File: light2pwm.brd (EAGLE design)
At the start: 55.5 x 47 mm, 8 parts, among them IC2 QUAD_OPAMPP

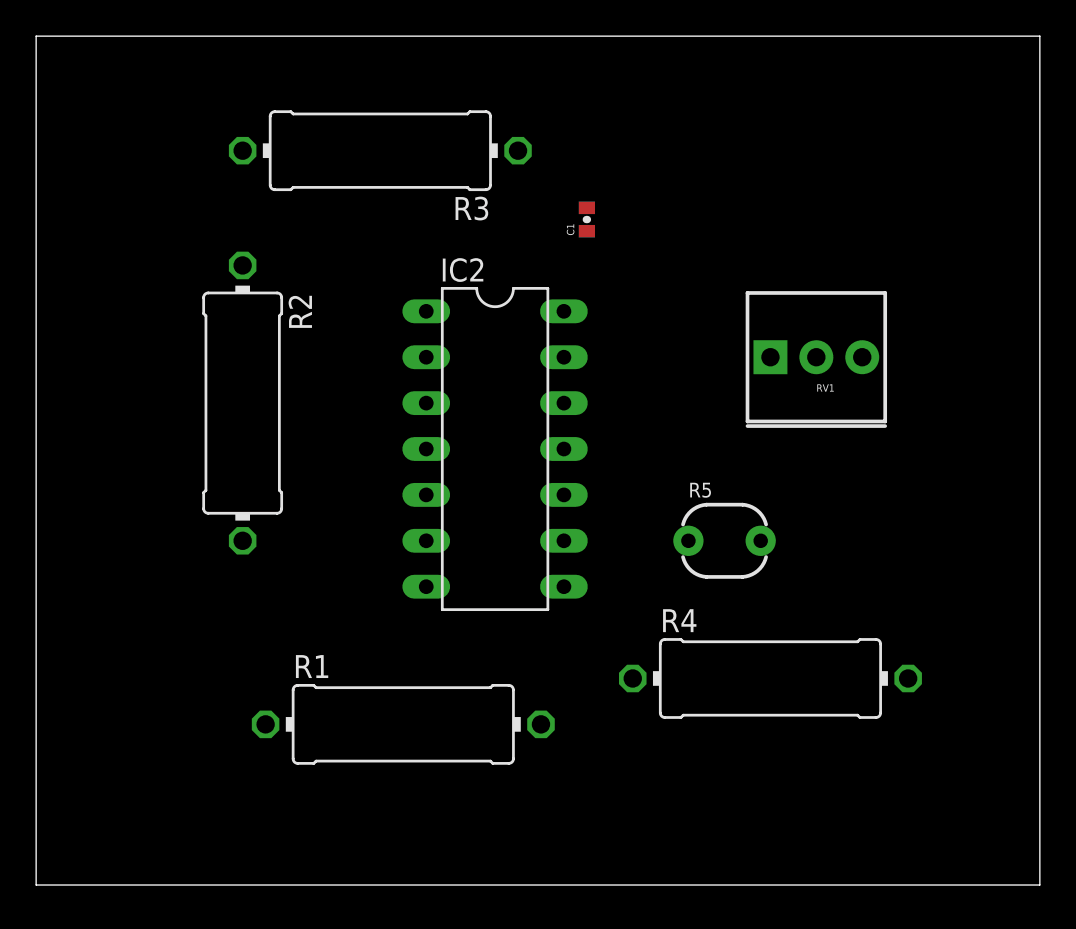
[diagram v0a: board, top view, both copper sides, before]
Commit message: pwm output pin added, next add transistor
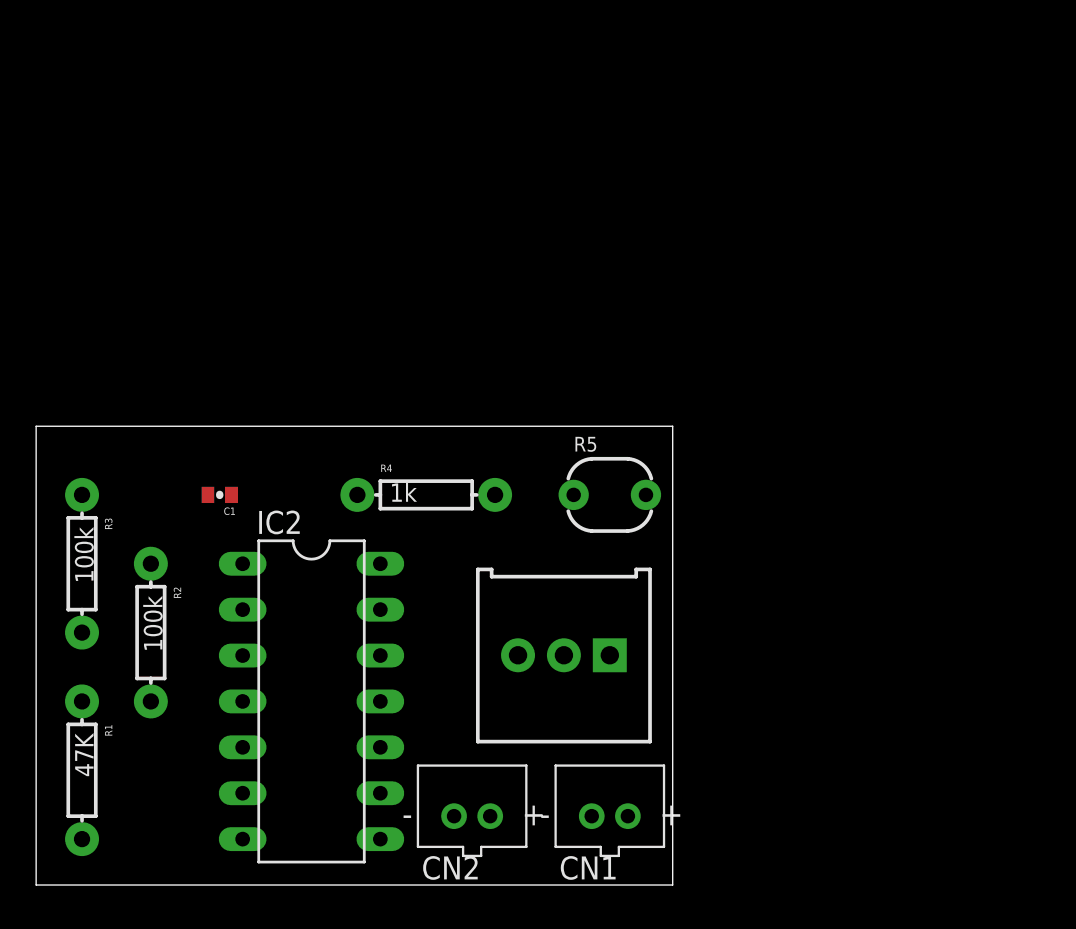
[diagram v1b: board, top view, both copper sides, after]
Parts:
- removed RV1: 10k, SparkFun-Electromechanical:3362U
- added CN1, CN2: (no value), adafruit:JST-PH-2-THM
- added R6: 10K, SparkFun-Electromechanical:3386U
- R1, R2, R3, R4: device adafruit:0414/15 -> SparkFun-Resistors:AXIAL-0.3EZ
- moved R3 28.2 mm to (2.54, 17.8), turned to 270 degrees
- moved C1 25.4 mm to (10.2, 21.6), turned to 180 degrees
- moved R4 21.6 mm to (21.6, 21.6)
- moved R1 18.0 mm to (2.54, 6.35), turned to 270 degrees
- moved IC2 17.3 mm to (15.2, 10.2)
- moved R2 13.7 mm to (6.35, 14.0)
- moved R5 6.84 mm to (31.8, 21.6)
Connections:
- new net N$7: CN2.2, IC2.8
- net GND: now also CN1.1, CN2.1, R4.P$2, R6.3; no longer R4.2, RV1.P$3
- net N$1: now also R1.P$1, R2.P$2; no longer R1.1, R2.2
- net N$2: now also R1.P$2; no longer R1.2
- net N$3: now also R2.P$1, R3.P$2; no longer R2.1, R3.2
- net N$4: now also R6.2; no longer RV1.P$2
- net N$5: now also R3.P$1; no longer R3.1
- net N$8: now also R4.P$1; no longer R4.1
- net VCC: now also CN1.2, R6.1; no longer RV1.P$1
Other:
- board size 55.5 x 47 mm -> 35.2 x 25.4 mm
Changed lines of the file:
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@@
 <board>
 <plain>
-<wire x1="0" y1="0" x2="55.55" y2="0" width="0" layer="20"/>
-<wire x1="55.55" y1="0" x2="55.55" y2="46.98" width="0" layer="20"/>
-<wire x1="55.55" y1="46.98" x2="0" y2="46.98" width="0" layer="20"/>
-<wire x1="0" y1="46.98" x2="0" y2="0" width="0" layer="20"/>
+<wire x1="0" y1="0" x2="35.23" y2="0" width="0" layer="20"/>
+<wire x1="35.23" y1="0" x2="35.23" y2="25.39" width="0" layer="20"/>
+<wire x1="35.23" y1="25.39" x2="0" y2="25.39" width="0" layer="20"/>
+<wire x1="0" y1="25.39" x2="0" y2="0" width="0" layer="20"/>
 </plain>
 <attributes>
@@
 </autorouter>
 <elements>
-<element name="C1" library="SparkFun-Retired" package="0402-CAP" value="10nF" x="30.48" y="36.83" rot="R90">
-<attribute name="PROD_ID" value="CAP-00867" x="30.48" y="36.83" size="1.778" layer="27" rot="R90" display="off"/>
+<element name="C1" library="SparkFun-Retired" package="0402-CAP" value="10nF" x="10.16" y="21.59" rot="R180">
+<attribute name="PROD_ID" value="CAP-00867" x="10.16" y="21.59" size="1.778" layer="27" rot="R180" display="off"/>
 </element>
-<element name="IC2" library="adafruit" package="DIL14" value="QUAD_OPAMPP" x="25.4" y="24.13" rot="R270"/>
-<element name="R1" library="adafruit" package="0414/15" value="47K" x="20.32" y="8.89"/>
-<element name="R2" library="adafruit" package="0414/15" value="100k" x="11.43" y="26.67" rot="R270"/>
-<element name="R3" library="adafruit" package="0414/15" value="100k" x="19.05" y="40.64" rot="R180"/>
-<element name="R4" library="adafruit" package="0414/15" value="1k" x="40.64" y="11.43"/>
-<element name="R5" library="SparkFun-Sensors" package="PHOTOCELL" value="PHOTOCELLPTH" x="38.1" y="19.05"/>
-<element name="RV1" library="SparkFun-Electromechanical" package="3362U" value="10k" x="40.64" y="26.67"/>
+<element name="IC2" library="adafruit" package="DIL14" value="QUAD_OPAMPP" x="15.24" y="10.16" rot="R270"/>
+<element name="R1" library="SparkFun-Resistors" package="AXIAL-0.3EZ" value="47K" x="2.54" y="6.35" rot="R270"/>
+<element name="R2" library="SparkFun-Resistors" package="AXIAL-0.3EZ" value="100k" x="6.35" y="13.97" rot="R270"/>
+<element name="R3" library="SparkFun-Resistors" package="AXIAL-0.3EZ" value="100k" x="2.54" y="17.78" rot="R270"/>
+<element name="R4" library="SparkFun-Resistors" package="AXIAL-0.3EZ" value="1k" x="21.59" y="21.59"/>
+<element name="R5" library="SparkFun-Sensors" package="PHOTOCELL" value="PHOTOCELLPTH" x="31.75" y="21.59"/>
+<element name="R6" library="SparkFun-Electromechanical" package="3386U" value="10K" x="29.21" y="12.7" rot="R180"/>
+<element name="CN1" library="adafruit" package="JST-PH-2-THM" value="" x="31.75" y="3.81"/>
+<element name="CN2" library="adafruit" package="JST-PH-2-THM" value="" x="24.13" y="3.81"/>
 </elements>
 <signals>
@@
 <signal name="N$1">
 <contactref element="IC2" pad="3"/>
-<contactref element="R1" pad="1"/>
-<contactref element="R2" pad="2"/>
-<wire x1="11.43" y1="19.05" x2="21.59" y2="26.67" width="0" layer="19" extent="1-1"/>
-<wire x1="12.7" y1="8.89" x2="11.43" y2="19.05" width="0" layer="19" extent="1-1"/>
+<contactref element="R1" pad="P$1"/>
+<contactref element="R2" pad="P$2"/>
+<wire x1="6.35" y1="10.16" x2="11.43" y2="12.7" width="0" layer="19" extent="1-1"/>
+<wire x1="2.54" y1="10.16" x2="6.35" y2="10.16" width="0" layer="19" extent="1-1"/>
 </signal>
 <signal name="N$2">
 <contactref element="IC2" pad="7"/>
-<contactref element="R1" pad="2"/>
+<contactref element="R1" pad="P$2"/>
 <contactref element="C1" pad="1"/>
 <contactref element="IC2" pad="10"/>
-<wire x1="29.21" y1="21.59" x2="30.48" y2="36.18" width="0" layer="19" extent="1-1"/>
-<wire x1="21.59" y1="16.51" x2="29.21" y2="21.59" width="0" layer="19" extent="1-1"/>
-<wire x1="27.94" y1="8.89" x2="21.59" y2="16.51" width="0" layer="19" extent="1-1"/>
+<wire x1="19.05" y1="7.62" x2="10.81" y2="21.59" width="0" layer="19" extent="1-1"/>
+<wire x1="11.43" y1="2.54" x2="19.05" y2="7.62" width="0" layer="19" extent="1-1"/>
+<wire x1="2.54" y1="2.54" x2="11.43" y2="2.54" width="0" layer="19" extent="1-1"/>
 </signal>
 <signal name="N$3">
 <contactref element="IC2" pad="1"/>
-<contactref element="R2" pad="1"/>
-<contactref element="R3" pad="2"/>
-<wire x1="11.43" y1="34.29" x2="11.43" y2="40.64" width="0" layer="19" extent="1-1"/>
-<wire x1="21.59" y1="31.75" x2="11.43" y2="34.29" width="0" layer="19" extent="1-1"/>
+<contactref element="R2" pad="P$1"/>
+<contactref element="R3" pad="P$2"/>
+<wire x1="6.35" y1="17.78" x2="11.43" y2="17.78" width="0" layer="19" extent="1-1"/>
+<wire x1="2.54" y1="13.97" x2="6.35" y2="17.78" width="0" layer="19" extent="1-1"/>
 </signal>
 <signal name="N$4">
 <contactref element="IC2" pad="5"/>
-<contactref element="RV1" pad="P$2"/>
 <contactref element="IC2" pad="2"/>
-<wire x1="21.59" y1="29.21" x2="43.18" y2="29.21" width="0" layer="19" extent="1-1"/>
-<wire x1="21.59" y1="21.59" x2="21.59" y2="29.21" width="0" layer="19" extent="1-1"/>
+<contactref element="R6" pad="2"/>
+<wire x1="11.43" y1="15.24" x2="29.21" y2="12.715" width="0" layer="19" extent="1-1"/>
+<wire x1="11.43" y1="7.62" x2="11.43" y2="15.24" width="0" layer="19" extent="1-1"/>
 </signal>
 <signal name="VCC">
-<contactref element="RV1" pad="P$1"/>
 <contactref element="R5" pad="2"/>
-<wire x1="40.1" y1="19.05" x2="40.64" y2="29.21" width="0" layer="19" extent="1-1"/>
+<contactref element="R6" pad="1"/>
+<contactref element="CN1" pad="2"/>
+<wire x1="31.75" y1="12.715" x2="33.75" y2="21.59" width="0" layer="19" extent="1-1"/>
+<wire x1="30.75" y1="3.81" x2="31.75" y2="12.715" width="0" layer="19" extent="1-1"/>
 </signal>
 <signal name="GND">
-<contactref element="RV1" pad="P$3"/>
-<contactref element="R4" pad="2"/>
-<wire x1="48.26" y1="11.43" x2="45.72" y2="29.21" width="0" layer="19" extent="1-1"/>
+<contactref element="R4" pad="P$2"/>
+<contactref element="R6" pad="3"/>
+<contactref element="CN1" pad="1"/>
+<contactref element="CN2" pad="1"/>
+<wire x1="26.67" y1="12.715" x2="25.4" y2="21.59" width="0" layer="19" extent="1-1"/>
+<wire x1="25.13" y1="3.81" x2="26.67" y2="12.715" width="0" layer="19" extent="1-1"/>
+<wire x1="32.75" y1="3.81" x2="25.13" y2="3.81" width="0" layer="19" extent="1-1"/>
 </signal>
 <signal name="N$5">
 <contactref element="IC2" pad="6"/>
-<contactref element="R3" pad="1"/>
+<contactref element="R3" pad="P$1"/>
 <contactref element="C1" pad="2"/>
-<wire x1="30.48" y1="37.48" x2="26.67" y2="40.64" width="0" layer="19" extent="1-1"/>
-<wire x1="21.59" y1="19.05" x2="30.48" y2="37.48" width="0" layer="19" extent="1-1"/>
+<wire x1="2.54" y1="21.59" x2="9.51" y2="21.59" width="0" layer="19" extent="1-1"/>
+<wire x1="11.43" y1="5.08" x2="9.51" y2="21.59" width="0" layer="19" extent="1-1"/>
 </signal>
 <signal name="N$8">
-<contactref element="R4" pad="1"/>
+<contactref element="R4" pad="P$1"/>
 <contactref element="R5" pad="1"/>
 <contactref element="IC2" pad="9"/>
-<wire x1="29.21" y1="19.05" x2="36.1" y2="19.05" width="0" layer="19" extent="1-1"/>
-<wire x1="33.02" y1="11.43" x2="36.1" y2="19.05" width="0" layer="19" extent="1-1"/>
+<wire x1="17.78" y1="21.59" x2="29.75" y2="21.59" width="0" layer="19" extent="1-1"/>
+<wire x1="19.05" y1="5.08" x2="17.78" y2="21.59" width="0" layer="19" extent="1-1"/>
+</signal>
+<signal name="N$7">
+<contactref element="IC2" pad="8"/>
+<contactref element="CN2" pad="2"/>
+<wire x1="19.05" y1="2.54" x2="23.13" y2="3.81" width="0" layer="19" extent="1-1"/>
 </signal>
 </signals>
